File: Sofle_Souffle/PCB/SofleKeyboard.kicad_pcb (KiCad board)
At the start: 2 copper layers, 143.3 x 111.7 mm, 94 parts, among them J2 4PIN, J3 OLED, P3 i2c_pin, P4 i2c_pin, P5 i2c_pin, P6 i2c_pin, P7 i2c_pin, SW1 SW_PUSH-MX_W_LED, SW10 SW_PUSH-MX_W_LED, SW11 SW_PUSH-MX_W_LED, SW12 SW_PUSH-MX_W_LED, SW13 SW_PUSH-MX_W_LED, SW14 SW_PUSH-MX_W_LED, SW15 SW_PUSH-MX_W_LED, SW16 SW_PUSH-MX_W_LED, SW17 SW_PUSH-MX_W_LED, SW18 SW_PUSH-MX_W_LED, SW19 SW_PUSH-MX_W_LED, SW2 SW_PUSH-MX_W_LED, SW20 SW_PUSH-MX_W_LED, SW21 SW_PUSH-MX_W_LED, SW22 SW_PUSH-MX_W_LED, SW23 SW_PUSH-MX_W_LED, SW24 SW_PUSH-MX_W_LED, SW25 Rotary_Encoder_Switch, SW25A1 SW_PUSH-MX_W_LED, SW26 SW_PUSH-MX_W_LED, SW27 SW_PUSH-MX_W_LED, SW28 SW_PUSH-MX_W_LED, SW29 SW_PUSH-MX_W_LED, SW3 SW_PUSH-MX_W_LED, SW30 SW_PUSH-MX_W_LED, SW4 SW_PUSH-MX_W_LED, SW5 SW_PUSH-MX_W_LED, SW6 SW_PUSH-MX_W_LED, SW7 SW_PUSH-MX_W_LED, SW8 SW_PUSH-MX_W_LED, SW9 SW_PUSH-MX_W_LED, U1 ProMicro

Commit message: Soufflé checkpoint commit.
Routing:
- net SW25A: track 188.9 -> 184.4 mm
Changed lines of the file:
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@@
   (via (at 137.287 122.428) (size 0.4) (drill 0.3) (layers "F.Cu" "B.Cu") (net 36))
   (via (at 118.11 128.27) (size 0.4) (drill 0.3) (layers "F.Cu" "B.Cu") (net 36))
-  (via (at 87.834 81.33) (size 0.4) (drill 0.3) (layers "F.Cu" "B.Cu") (net 36))
+  (via (at 87.834 78.232) (size 0.4) (drill 0.3) (layers "F.Cu" "B.Cu") (net 36))
   (via (at 174.6885 65.2145) (size 0.4) (drill 0.3) (layers "F.Cu" "B.Cu") (net 36))
   (via (at 116.84 63.754) (size 0.4) (drill 0.3) (layers "F.Cu" "B.Cu") (net 36))
-  (via (at 85.344 82.042) (size 0.4) (drill 0.3) (layers "F.Cu" "B.Cu") (net 36))
+  (via (at 85.598 82.55) (size 0.4) (drill 0.3) (layers "F.Cu" "B.Cu") (net 36))
   (via (at 108.712 84.836) (size 0.4) (drill 0.3) (layers "F.Cu" "B.Cu") (net 36))
   (via (at 82.55 78.994) (size 0.4) (drill 0.3) (layers "F.Cu" "B.Cu") (net 36))
-  (segment (start 87.834 81.33) (end 87.834 74.472) (width 0.5) (layer "B.Cu") (net 36))
+  (segment (start 87.834 74.472) (end 87.884 74.422) (width 0.5) (layer "B.Cu") (net 36))
   (segment (start 87.834 84.768) (end 87.834 90.718) (width 0.5) (layer "B.Cu") (net 36))
   (segment (start 89.916 74.168) (end 89.916 47.39) (width 0.5) (layer "B.Cu") (net 36))
+  (segment (start 87.834 84.768) (end 87.834 78.232) (width 0.5) (layer "B.Cu") (net 36))
   (segment (start 88.963758 74.422) (end 89.217758 74.168) (width 0.5) (layer "B.Cu") (net 36))
   (segment (start 84.634 74.422) (end 83.312 75.744) (width 0.5) (layer "B.Cu") (net 36))
   (segment (start 89.217758 74.168) (end 89.916 74.168) (width 0.5) (layer "B.Cu") (net 36))
   (segment (start 89.916 47.39) (end 89.920255 47.385745) (width 0.5) (layer "B.Cu") (net 36))
-  (segment (start 87.834 74.472) (end 87.884 74.422) (width 0.5) (layer "B.Cu") (net 36))
+  (segment (start 87.834 78.232) (end 87.834 74.472) (width 0.5) (layer "B.Cu") (net 36))
   (segment (start 84.634 74.422) (end 87.884 74.422) (width 0.5) (layer "B.Cu") (net 36))
   (segment (start 89.916 74.168) (end 91.328001 72.755999) (width 0.5) (layer "B.Cu") (net 36))
-  (segment (start 87.834 84.768) (end 87.834 81.33) (width 0.5) (layer "B.Cu") (net 36))
   (segment (start 87.884 74.422) (end 88.963758 74.422) (width 0.5) (layer "B.Cu") (net 36))
   (segment (start 101.346 82.296) (end 102.616 83.566) (width 0.5) (layer "F.Cu") (net 37))
@@
   (segment (start 86.712815 49.925745) (end 85.149493 49.925745) (width 0.25) (layer "B.Cu") (net 46))
   (segment (start 85.149493 49.925745) (end 84.291853 50.783385) (width 0.25) (layer "B.Cu") (net 46))
+  (segment (start 109.474 98.044) (end 109.982 97.536) (width 0.25) (layer "F.Cu") (net 47))
   (segment (start 98.089977 71.730979) (end 99.144743 72.785745) (width 0.25) (layer "F.Cu") (net 47))
   (segment (start 98.918 113.304) (end 96.963489 115.258511) (width 0.25) (layer "F.Cu") (net 47))
@@
   (segment (start 119.90038 57.30938) (end 120.182181 57.591181) (width 0.25) (layer "F.Cu") (net 47))
   (segment (start 104.14 73.152) (end 104.14 73.929002) (width 0.25) (layer "F.Cu") (net 47))
+  (segment (start 102.069489 92.417489) (end 107.696 98.044) (width 0.25) (layer "F.Cu") (net 47))
   (segment (start 119.52718 76.35938) (end 117.65456 78.232) (width 0.25) (layer "F.Cu") (net 47))
   (segment (start 102.344999 116.857001) (end 98.918 113.430002) (width 0.25) (layer "F.Cu") (net 47))
   (segment (start 120.182181 57.591181) (end 120.182181 75.704379) (width 0.25) (layer "F.Cu") (net 47))
-  (segment (start 99.06 89.916) (end 102.362 89.916) (width 0.25) (layer "F.Cu") (net 47))
   (segment (start 117.65456 59.182) (end 109.982 59.182) (width 0.25) (layer "F.Cu") (net 47))
+  (segment (start 97.79 91.186) (end 99.021489 92.417489) (width 0.25) (layer "F.Cu") (net 47))
   (segment (start 119.52718 95.40938) (end 120.182181 94.754379) (width 0.25) (layer "F.Cu") (net 47))
   (segment (start 120.182181 94.754379) (end 120.182181 77.014381) (width 0.25) (layer "F.Cu") (net 47))
   (segment (start 109.456999 116.857001) (end 102.344999 116.857001) (width 0.25) (layer "F.Cu") (net 47))
-  (segment (start 97.79 91.186) (end 99.06 89.916) (width 0.25) (layer "F.Cu") (net 47))
   (segment (start 117.65456 116.332) (end 109.982 116.332) (width 0.25) (layer "F.Cu") (net 47))
   (segment (start 119.52718 57.30938) (end 119.90038 57.30938) (width 0.25) (layer "F.Cu") (net 47))
   (segment (start 119.52718 114.45938) (end 117.65456 116.332) (width 0.25) (layer "F.Cu") (net 47))
   (segment (start 98.918 113.430002) (end 98.918 112.054) (width 0.25) (layer "F.Cu") (net 47))
+  (segment (start 107.696 98.044) (end 109.474 98.044) (width 0.25) (layer "F.Cu") (net 47))
   (segment (start 120.182181 113.804379) (end 120.182181 96.064381) (width 0.25) (layer "F.Cu") (net 47))
-  (segment (start 102.362 89.916) (end 109.982 82.296) (width 0.25) (layer "F.Cu") (net 47))
+  (segment (start 109.982 97.536) (end 109.982 97.282) (width 0.25) (layer "F.Cu") (net 47))
   (segment (start 109.982 116.332) (end 109.456999 116.857001) (width 0.25) (layer "F.Cu") (net 47))
   (segment (start 99.458255 72.785745) (end 100.654 71.59) (width 0.25) (layer "F.Cu") (net 47))
@@
   (segment (start 92.042511 115.258511) (end 90.718 113.934) (width 0.25) (layer "F.Cu") (net 47))
   (segment (start 119.52718 95.40938) (end 117.65456 97.282) (width 0.25) (layer "F.Cu") (net 47))
+  (segment (start 99.021489 92.417489) (end 102.069489 92.417489) (width 0.25) (layer "F.Cu") (net 47))
   (segment (start 120.182181 96.064381) (end 119.52718 95.40938) (width 0.25) (layer "F.Cu") (net 47))
   (segment (start 96.963489 115.258511) (end 92.042511 115.258511) (width 0.25) (layer "F.Cu") (net 47))
   (segment (start 108.967999 78.757001) (end 109.456999 78.757001) (width 0.25) (layer "F.Cu") (net 47))
   (segment (start 120.182181 77.014381) (end 119.52718 76.35938) (width 0.25) (layer "F.Cu") (net 47))
-  (segment (start 109.982 82.296) (end 109.982 78.232) (width 0.25) (layer "F.Cu") (net 47))
   (via (at 109.982 78.232) (size 0.4) (drill 0.3) (layers "F.Cu" "B.Cu") (net 47))
   (via (at 109.982 116.332) (size 0.4) (drill 0.3) (layers "F.Cu" "B.Cu") (net 47))

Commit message: Checkpoint commit.
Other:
- outline, holes or cut-outs redrawn
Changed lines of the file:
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@@
   (setup
     (pad_to_mask_clearance 0)
-    (grid_origin 90.424 80.01)
+    (grid_origin 93.218 106.934)
     (pcbplotparams
       (layerselection 0x00010fc_ffffffff)
@@
     (fp_line (start 5.9 -1.1) (end 2.62 -1.1) (layer "F.SilkS") (width 0.15))
     (fp_line (start 5.67 -3.7) (end 5.67 -1.46) (layer "F.SilkS") (width 0.15))
-    (fp_arc (start 0.8 -3.4) (mid 2.26871 -2.886118) (end 3.016318 -1.521471) (layer "F.SilkS") (width 1))
+    (fp_arc (start 0.8 -3.4) (mid 2.268709 -2.886118) (end 3.016318 -1.521471) (layer "F.SilkS") (width 1))
     (fp_arc (start 0.4 -3) (mid 1.868709 -2.486118) (end 2.616318 -1.121471) (layer "F.SilkS") (width 0.15))
     (fp_arc (start 3.8 -6.600001) (mid 5.243504 -6.084925) (end 5.900001 -4.7) (layer "F.SilkS") (width 0.15))
@@
     )
   )
-  (gr_line (start 218.769181 46.770902) (end 218.768802 139.879974) (layer "Cmts.User") (width 0.1))
-  (gr_arc (start 218.768802 139.879974) (mid 218.600311 140.284023) (end 218.194741 140.448819) (layer "Cmts.User") (width 0.1))
-  (gr_line (start 218.194741 140.448819) (end 199.4343 140.44882) (layer "Cmts.User") (width 0.1))
+  (gr_line (start 218.769181 46.770902) (end 218.768802 139.625974) (layer "Cmts.User") (width 0.1))
+  (gr_line (start 217.940741 140.448819) (end 199.4343 140.44882) (layer "Cmts.User") (width 0.1))
   (gr_line (start 218.352621 45.8846) (end 218.494321 46.024582) (layer "Cmts.User") (width 0.1))
   (gr_line (start 142.326 37.189) (end 164.276 37.189) (layer "Cmts.User") (width 0.1))
@@
   (gr_line (start 131.480128 136.189) (end 180.826 136.189) (layer "Cmts.User") (width 0.1))
   (gr_line (start 87.112 148.905) (end 87.54872 148.85416) (layer "Cmts.User") (width 0.1))
+  (gr_arc (start 218.768802 139.625974) (mid 218.526451 140.210164) (end 217.940741 140.448819) (layer "Cmts.User") (width 0.1))
   (gr_line (start 131.480128 136.189) (end 180.826 136.189) (layer "Edge.Cuts") (width 0.1))
   (gr_line (start 199.4343 140.44882) (end 180.826 136.189) (layer "Edge.Cuts") (width 0.1))
@@
   (gr_line (start 218.750381 46.563571) (end 218.769181 46.770902) (layer "Edge.Cuts") (width 0.1))
   (gr_line (start 85.876 148.389) (end 75.626 130.589) (layer "Edge.Cuts") (width 0.1))
-  (gr_line (start 218.194741 140.448819) (end 199.4343 140.44882) (layer "Edge.Cuts") (width 0.1))
-  (gr_arc (start 218.768802 139.879974) (mid 218.600311 140.284023) (end 218.194741 140.448819) (layer "Edge.Cuts") (width 0.1))
-  (gr_line (start 218.769181 46.770902) (end 218.768802 139.879974) (layer "Edge.Cuts") (width 0.1))
+  (gr_line (start 217.940741 140.448819) (end 199.4343 140.44882) (layer "Edge.Cuts") (width 0.1))
+  (gr_arc (start 218.768802 139.625974) (mid 218.5264 140.210113) (end 217.940741 140.448819) (layer "Edge.Cuts") (width 0.1))
+  (gr_line (start 218.769181 46.770902) (end 218.768802 139.625974) (layer "Edge.Cuts") (width 0.1))
   (gr_line (start 81.623257 40.434261) (end 81.690377 40.218014) (layer "Edge.Cuts") (width 0.1))
   (gr_line (start 164.276 37.189) (end 217.801441 45.634146) (layer "Edge.Cuts") (width 0.1))

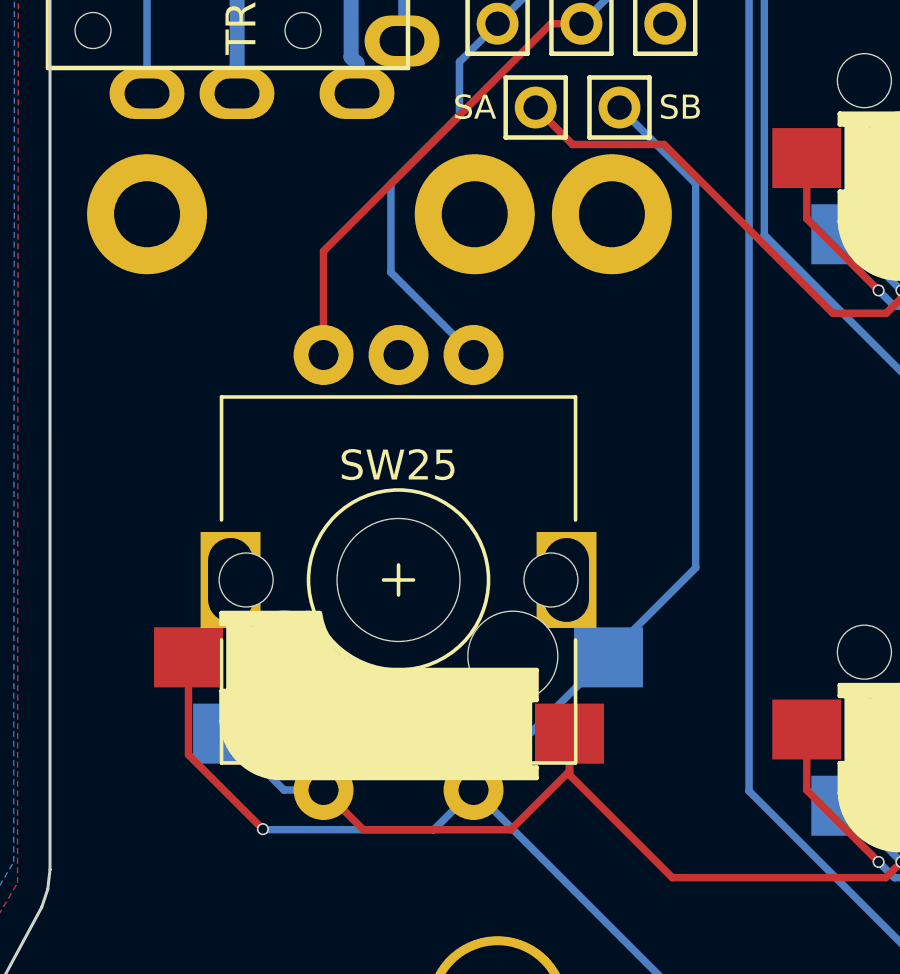
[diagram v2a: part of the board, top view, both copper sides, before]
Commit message: Updated PCB with corrected trace.
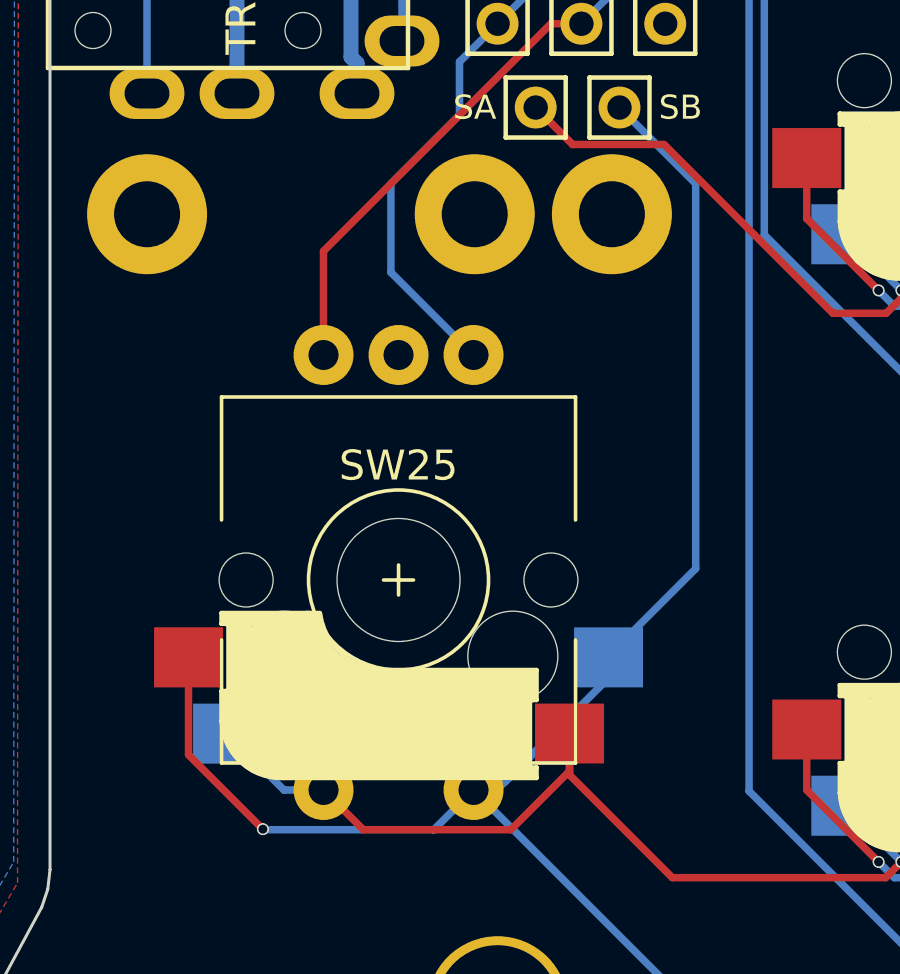
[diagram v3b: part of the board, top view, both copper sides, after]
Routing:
- net SW25B: track 69.6 -> 71.3 mm
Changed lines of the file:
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@@
     (pcbplotparams
       (layerselection 0x00010fc_ffffffff)
-      (disableapertmacros false)
-      (usegerberextensions false)
-      (usegerberattributes true)
-      (usegerberadvancedattributes true)
-      (creategerberjobfile true)
+      (disableapertmacros true)
+      (usegerberextensions true)
+      (usegerberattributes false)
+      (usegerberadvancedattributes false)
+      (creategerberjobfile false)
       (svguseinch false)
       (svgprecision 6)
@@
       (psa4output false)
       (plotreference true)
-      (plotvalue true)
+      (plotvalue false)
       (plotinvisibletext false)
       (sketchpadsonfab false)
-      (subtractmaskfromsilk false)
+      (subtractmaskfromsilk true)
       (outputformat 1)
       (mirror false)
-      (drillshape 1)
+      (drillshape 0)
       (scaleselection 1)
-      (outputdirectory "")
+      (outputdirectory "gerber/")
     )
   )
@@
     (fp_line (start -6 -4.7) (end -5 -5.8) (layer "F.Fab") (width 0.12))
     (fp_circle (center 0 0) (end 3 0) (layer "F.Fab") (width 0.12) (fill none))
+    (pad "" np_thru_hole oval locked (at 0 5.6 270) (size 2.8 1.5) (drill oval 2.8 1.5) (layers F&B.Cu *.Mask))
+    (pad "" np_thru_hole oval locked (at 0 -5.6 270) (size 2.8 1.5) (drill oval 2.8 1.5) (layers F&B.Cu *.Mask))
     (pad "A" thru_hole circle locked (at -7.5 -2.5 270) (size 2 2) (drill 1) (layers *.Cu *.Mask)
       (net 54 "ENCA") (pinfunction "A") (pintype "passive"))
@@
     (pad "C" thru_hole circle locked (at -7.5 0 270) (size 2 2) (drill 1) (layers *.Cu *.Mask)
       (net 36 "GND") (pinfunction "C") (pintype "passive"))
-    (pad "MP" thru_hole rect locked (at 0 5.6 270) (size 3.2 2) (drill oval 2.8 1.5) (layers *.Cu *.Mask))
-    (pad "MP" thru_hole rect locked (at 0 -5.6 270) (size 3.2 2) (drill oval 2.8 1.5) (layers *.Cu *.Mask))
     (pad "S1" thru_hole circle locked (at 7 2.5 270) (size 2 2) (drill 1) (layers *.Cu *.Mask)
       (net 47 "SW25A") (pinfunction "S1") (pintype "passive"))
@@
     (fp_line (start 5.9 -1.1) (end 2.62 -1.1) (layer "F.SilkS") (width 0.15))
     (fp_line (start 5.67 -3.7) (end 5.67 -1.46) (layer "F.SilkS") (width 0.15))
-    (fp_arc (start 0.8 -3.4) (mid 2.268709 -2.886118) (end 3.016318 -1.521471) (layer "F.SilkS") (width 1))
+    (fp_arc (start 0.8 -3.4) (mid 2.26871 -2.886118) (end 3.016318 -1.521471) (layer "F.SilkS") (width 1))
     (fp_arc (start 0.4 -3) (mid 1.868709 -2.486118) (end 2.616318 -1.121471) (layer "F.SilkS") (width 0.15))
     (fp_arc (start 3.8 -6.600001) (mid 5.243504 -6.084925) (end 5.900001 -4.7) (layer "F.SilkS") (width 0.15))
@@
   (gr_line (start 142.326 37.189) (end 82.751853 39.514405) (layer "Edge.Cuts") (width 0.1))
   (gr_line (start 87.112 148.905) (end 87.54872 148.85416) (layer "Edge.Cuts") (width 0.1))
+  (dimension (type orthogonal) (layer "Cmts.User")
+    (pts (xy 163.068 37.189) (xy 87.33036 148.87958))
+    (height -107.15625)
+    (orientation 1)
+    (gr_text "111.6906 mm" (at 54.76175 93.03429 90) (layer "Cmts.User")
+      (effects (font (size 1 1) (thickness 0.15)))
+    )
+    (format (units 3) (units_format 1) (precision 4))
+    (style (thickness 0.1) (arrow_length 1.27) (text_position_mode 0) (extension_height 0.58642) (extension_offset 0.5) keep_text_aligned)
+  )
+  (dimension (type orthogonal) (layer "Cmts.User")
+    (pts (xy 75.426 129.489) (xy 218.55034 129.95275))
+    (height 28.245)
+    (orientation 0)
+    (gr_text "143.1243 mm" (at 146.98817 156.584) (layer "Cmts.User")
+      (effects (font (size 1 1) (thickness 0.15)))
+    )
+    (format (units 3) (units_format 1) (precision 4))
+    (style (thickness 0.1) (arrow_length 1.27) (text_position_mode 0) (extension_height 0.58642) (extension_offset 0.5) keep_text_aligned)
+  )
   (segment (start 99.022 61.43) (end 99.06 61.468) (width 0.25) (layer "F.Cu") (net 1))
   (segment (start 85.414 61.43) (end 99.022 61.43) (width 0.25) (layer "F.Cu") (net 1))
@@
   (via (at 119.888 124.206) (size 0.4) (drill 0.3) (layers "F.Cu" "B.Cu") (net 30))
   (segment (start 94.393489 115.258511) (end 95.718 113.934) (width 0.25) (layer "B.Cu") (net 30))
-  (segment (start 103.124 93.726) (end 100.584 91.186) (width 0.25) (layer "B.Cu") (net 30))
-  (segment (start 103.124 106.528) (end 103.124 93.726) (width 0.25) (layer "B.Cu") (net 30))
+  (segment (start 103.124 106.553) (end 100.218 109.459) (width 0.25) (layer "B.Cu") (net 30))
+  (segment (start 96.488974 113.934) (end 96.765987 113.656987) (width 0.25) (layer "B.Cu") (net 30))
   (segment (start 119.888 124.206) (end 105.99 124.206) (width 0.25) (layer "B.Cu") (net 30))
+  (segment (start 96.765987 113.656987) (end 97.632521 112.790453) (width 0.25) (layer "B.Cu") (net 30))
   (segment (start 105.99 124.206) (end 95.718 113.934) (width 0.25) (layer "B.Cu") (net 30))
+  (segment (start 100.218 109.514) (end 100.218 110.204974) (width 0.25) (layer "B.Cu") (net 30))
+  (segment (start 103.124 93.726) (end 100.584 91.186) (width 0.25) (layer "B.Cu") (net 30))
+  (segment (start 100.218 110.204974) (end 96.765987 113.656987) (width 0.25) (layer "B.Cu") (net 30))
+  (segment (start 100.218 109.459) (end 100.218 109.514) (width 0.25) (layer "B.Cu") (net 30))
+  (segment (start 95.718 113.934) (end 96.488974 113.934) (width 0.25) (layer "B.Cu") (net 30))
   (segment (start 88.715511 115.258511) (end 94.393489 115.258511) (width 0.25) (layer "B.Cu") (net 30))
   (segment (start 88.6968 115.2398) (end 88.715511 115.258511) (width 0.25) (layer "B.Cu") (net 30))
-  (segment (start 95.718 113.934) (end 103.124 106.528) (width 0.25) (layer "B.Cu") (net 30))
+  (segment (start 103.124 106.553) (end 103.124 93.726) (width 0.25) (layer "B.Cu") (net 30))
   (segment (start 81.733298 135.012795) (end 82.585771 131.831322) (width 0.25) (layer "F.Cu") (net 31))
   (segment (start 82.585771 131.831322) (end 84.273654 130.856822) (width 0.25) (layer "F.Cu") (net 31))
